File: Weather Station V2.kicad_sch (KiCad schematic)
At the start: 44 parts, among them J1 SOLAR IN, J2 18650, J3 Battery_AUX, J6 USB_C, J7 RYLR998, J8 Breakout, Q1 AO4842, Q2 DMP2240UDM-7, SW1 LED_ENABLE, SW2 EN/RST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

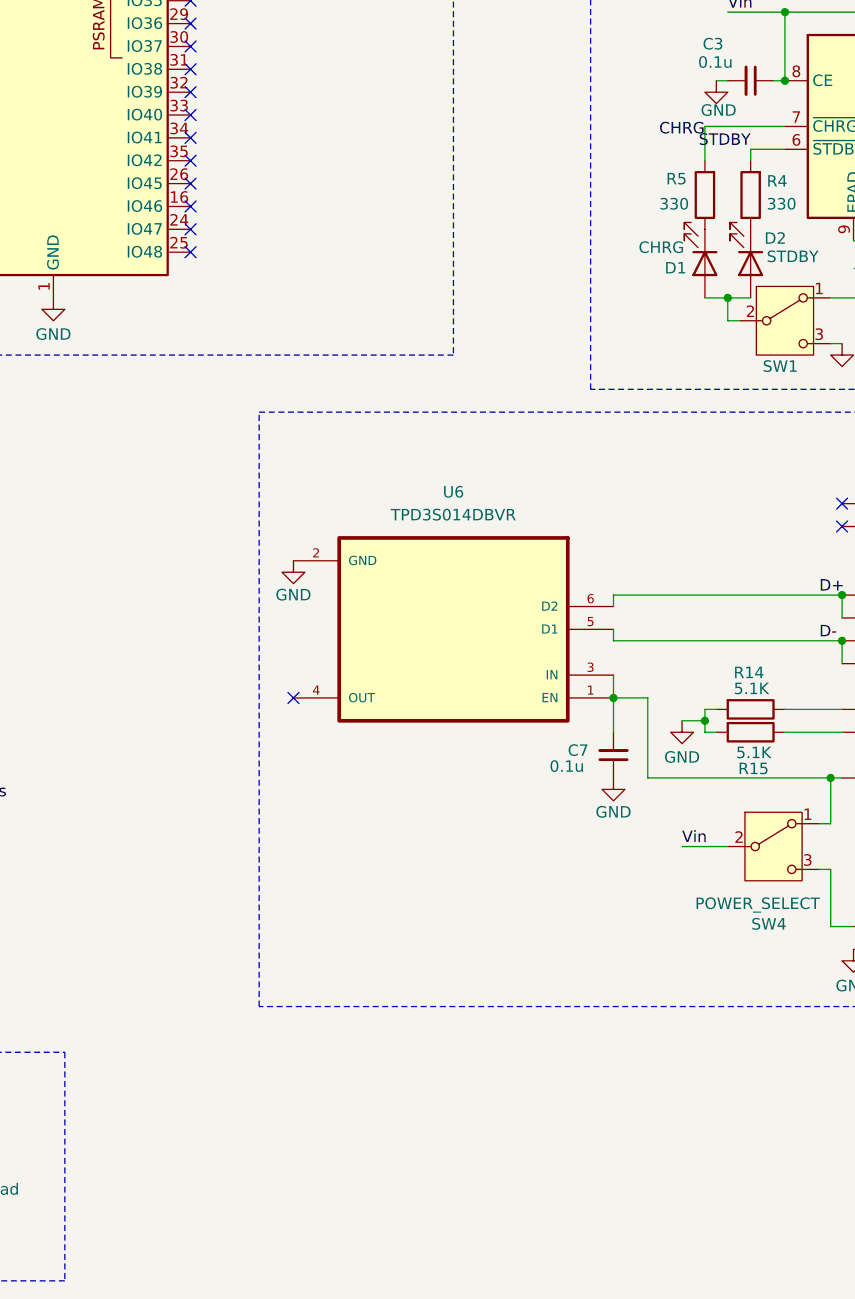
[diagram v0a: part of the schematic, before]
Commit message: Added esp32 connection to charging status lines (CHRG 48, STDBY 47) Panelization with breakout board. Potentially final. Proably sending it soon
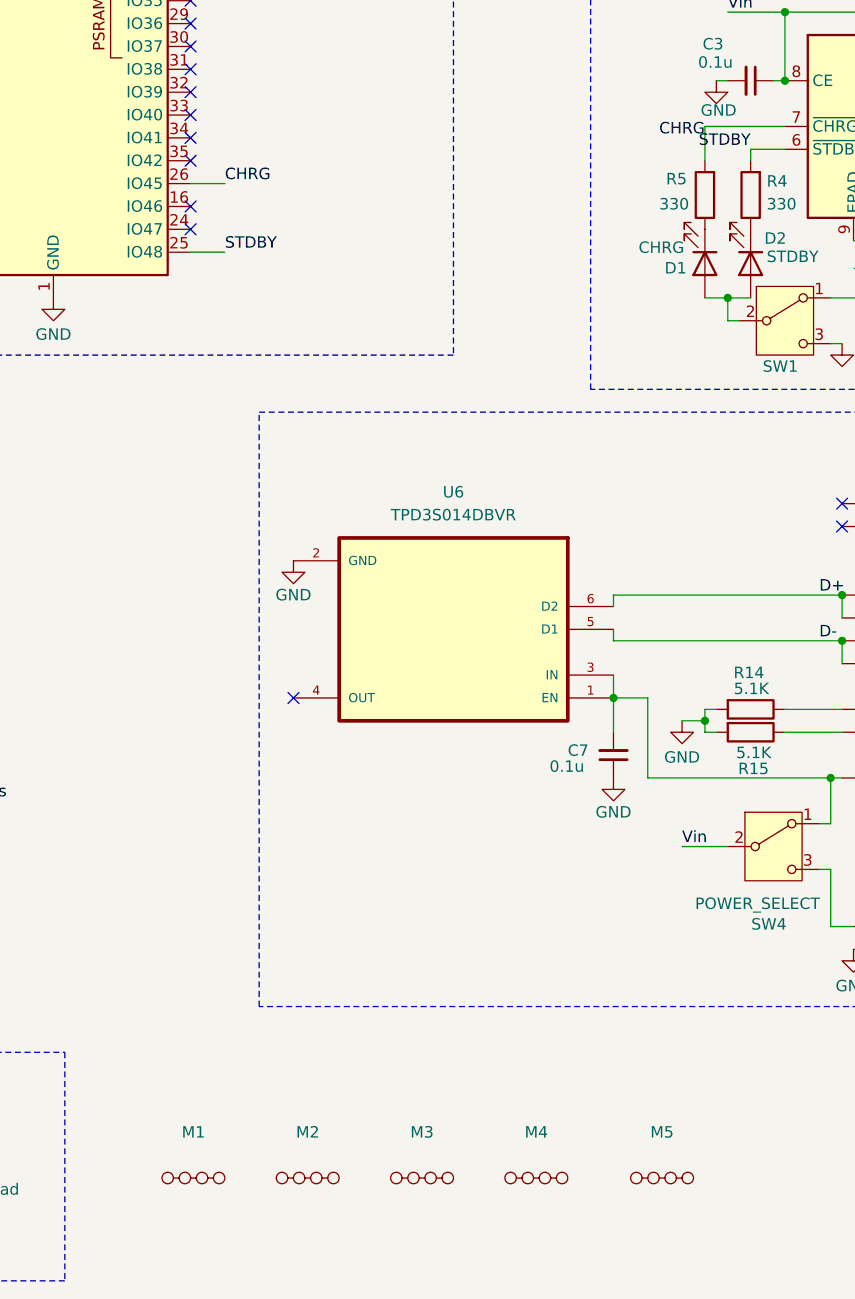
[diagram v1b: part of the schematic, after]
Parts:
- added M1, M2, M3, M4, M5: ~, PCM_JLCPCB:MouseBites, Cosmetic, JLCPCB, 1.6mm, symbol PCM_JLCPCB-Manufacturing:Mousebites, Cosmetic, 3mm
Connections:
- net CHRG: now also U5.26 (IO45)
- net STDBY: now also U5.25 (IO48)
- no-connect marks 22 -> 20

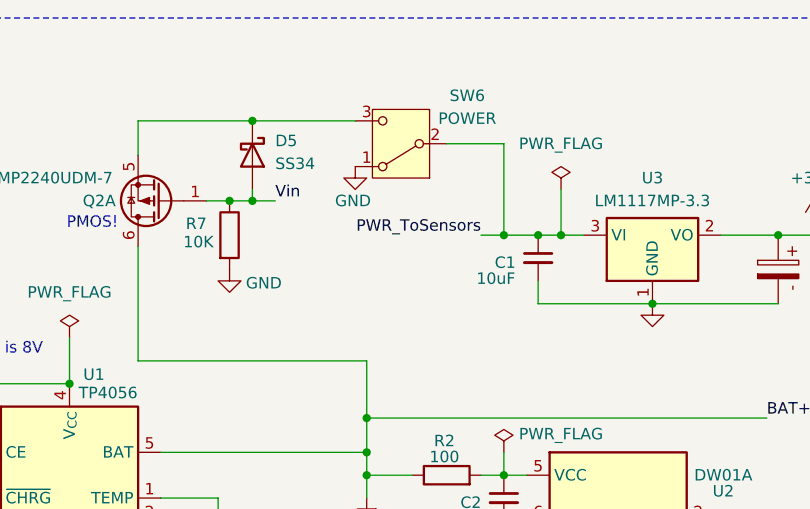
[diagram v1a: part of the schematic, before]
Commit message: Now sensor power gets switched before 5V boost-coverter Reduced 3.3v plane size
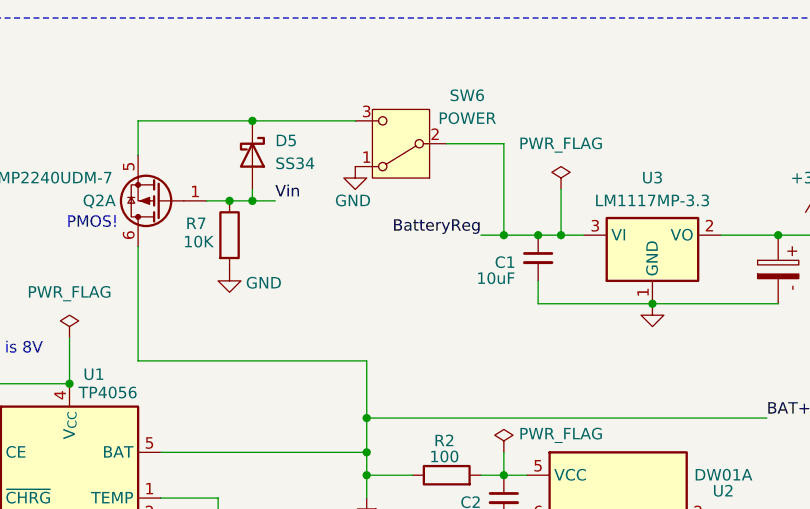
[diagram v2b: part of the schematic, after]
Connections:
- net PWR_ToSensors: no longer C1.1, SW6.2 (B), U3.3 (VI)
- new net BatteryReg: C1.1, SW6.2 (B), U3.3 (VI)
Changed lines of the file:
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@@
 		)
 	)
-	(label "PWR_ToSensors"
+	(label "BatteryReg"
 		(at 236.22 36.83 180)
 		(effects

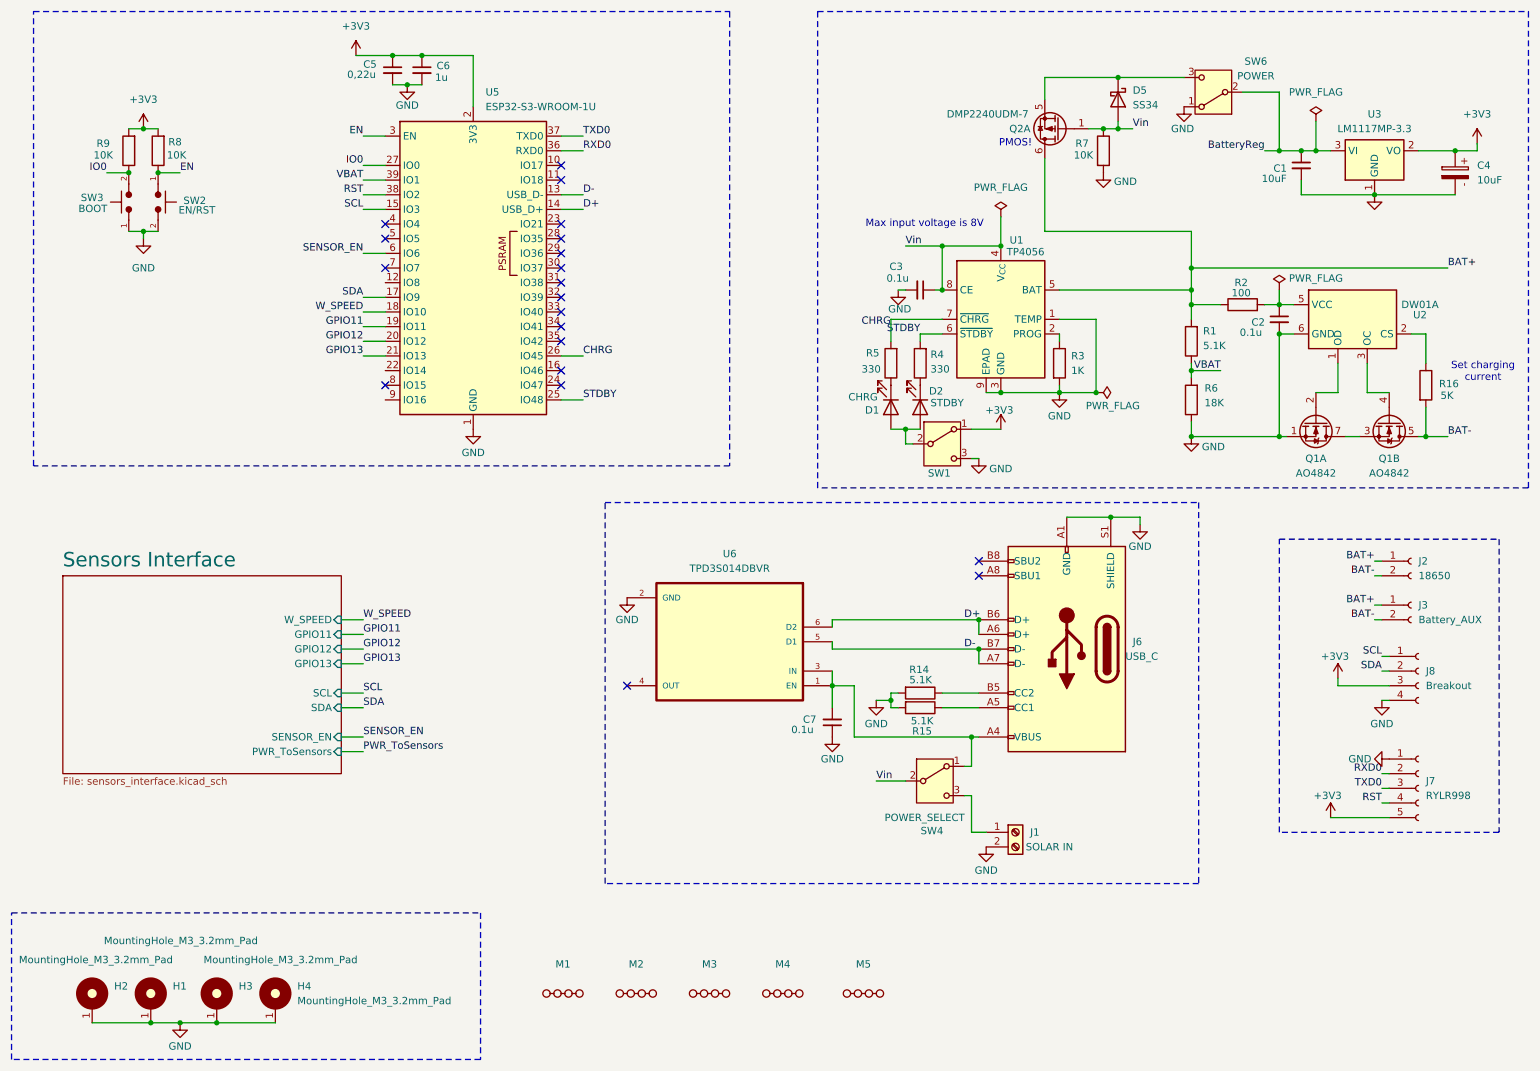
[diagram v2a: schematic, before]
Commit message: - Changed CHRG and STDBY pins to 48 and 47 (CHRG was strapping) - Exposed 5V rail do Breakout connector. Now also it matches a bme280 pinout for testing - Renamed BatteryReg net to Battery_SW - Fixed connection to 5V converter - Changed to USBLC6-2SC6 for ESD Protection - Fixed mirrored VEML7700 footprint
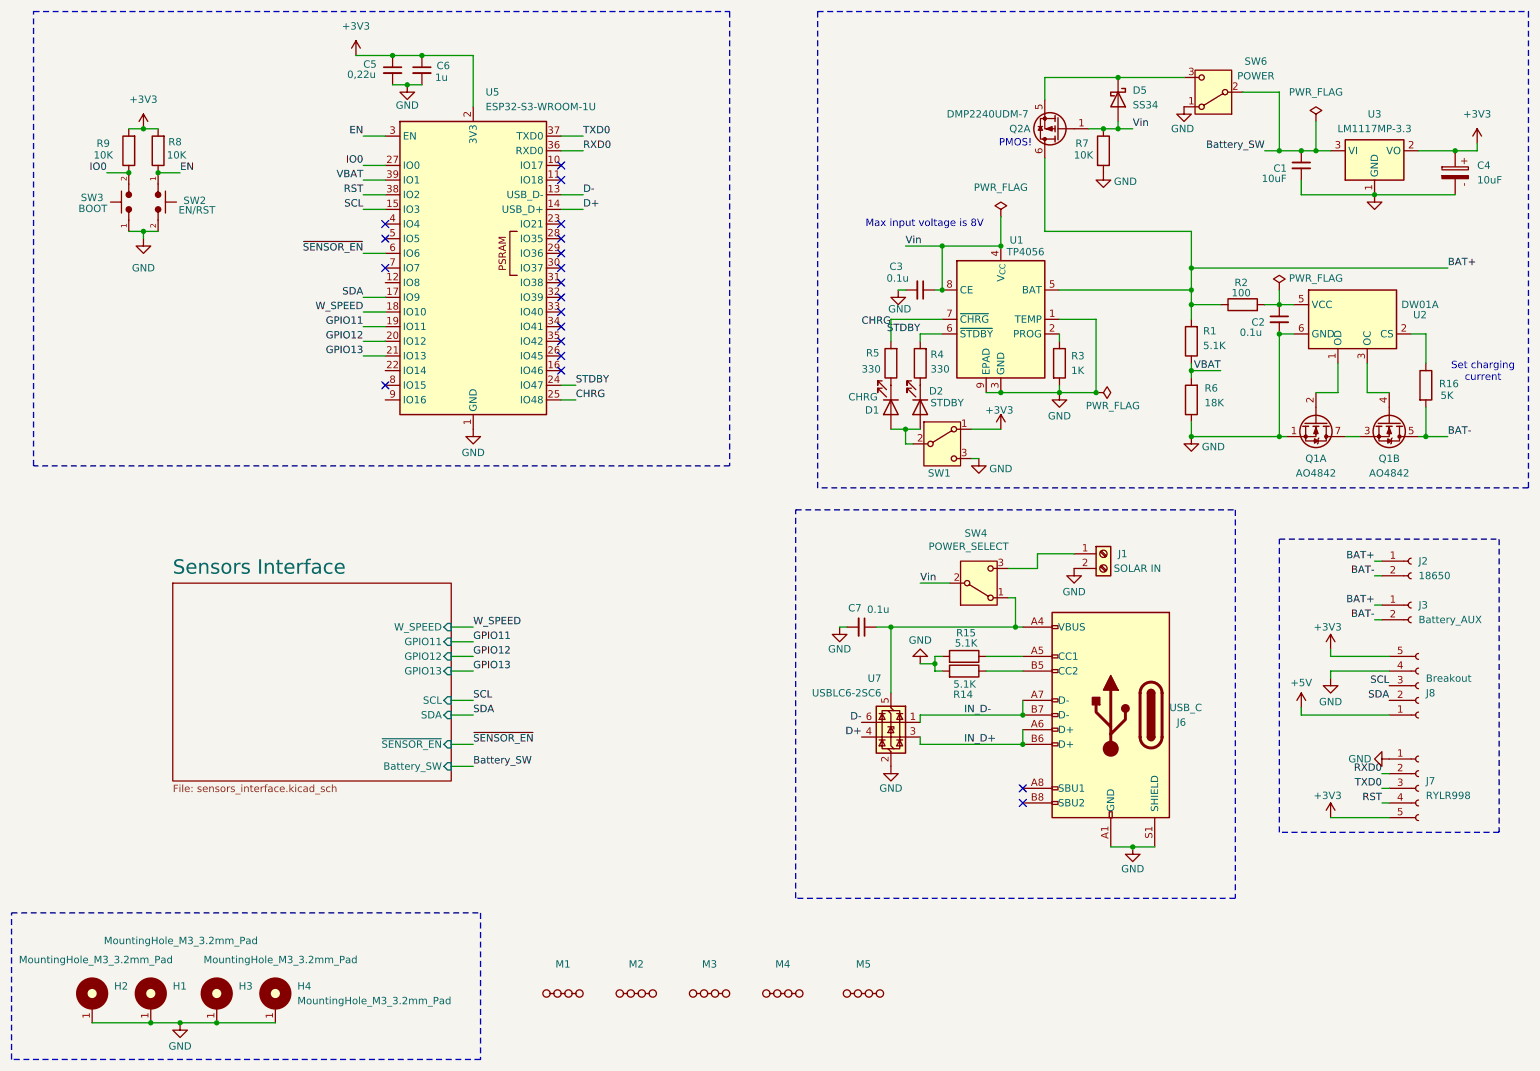
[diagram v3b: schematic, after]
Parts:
- removed J8: Breakout, Connector_PinSocket_2.54mm:PinSocket_1x04_P2.54mm_Vertical, symbol Connector:Conn_01x04_Socket
- removed U6: TPD3S014DBVR, TPD3S014DBVR:SOT95P280X145-6N, symbol TPD3S014DBVR:TPD3S014DBVR
- added J8: Breakout, Connector_PinSocket_2.54mm:PinSocket_1x05_P2.54mm_Vertical, symbol Connector:Conn_01x05_Socket
- added U7: USBLC6-2SC6, Package_TO_SOT_SMD:SOT-23-6, symbol Power_Protection:USBLC6-2SC6
- M1, M2, M3, M4, M5: value ~ -> (none)
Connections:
- net +3V3: now also J8.5 (Pin_5)
- net CHRG: now also U5.25 (IO48); no longer U5.26 (IO45)
- net D+: now also U7.4 (I/O2); no longer J6.A6 (D+), J6.B6 (D+)
- net D-: now also U7.6 (I/O1); no longer J6.A7 (D-), J6.B7 (D-)
- net GND: now also C7.2, J8.4 (Pin_4), U7.2 (GND); no longer C7.1
- net SCL: now also J8.3 (Pin_3)
- net SDA: now also J8.2 (Pin_2)
- net STDBY: now also U5.24 (IO47); no longer U5.25 (IO48)
- net at J6.A4 (VBUS), J6.A9 (VBUS), J6.B4 (VBUS)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: now also C7.1, U7.5 (VBUS); no longer C7.2
- net BatteryReg renamed Battery_SW
- net SENSOR_EN renamed ~{SENSOR_EN}
- new net +5V: J8.1 (Pin_1)
- new net IN_D+: J6.A6 (D+), J6.B6 (D+), U7.3 (I/O2)
- new net IN_D-: J6.A7 (D-), J6.B7 (D-), U7.1 (I/O1)
- no-connect marks 20 -> 19
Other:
- sheet Sensors Interface ports: added Battery_SW, ~{SENSOR_EN}; removed PWR_ToSensors, SENSOR_EN
- moved on the sheet: J1, J6, R14, R15, SW4

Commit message: - Changed 3V3 LDO to LDL1117S33R - In a previous commit ON OFF power lables were switched
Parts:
- removed C4: 10uF, Capacitor_THT:CP_Radial_D5.0mm_P2.00mm, symbol PCM_SL_Capacitors:10uF_50V
- added C4: 4.7uF, Capacitor_SMD:C_1206_3216Metric, symbol Device:C_Small
- U3: value LM1117MP-3.3 -> LDL1117S33R
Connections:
- net +3V3: now also C4.1
- net GND: now also C4.2
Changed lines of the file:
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@@
 	)
 	(junction
-		(at 269.24 36.83)
-		(diameter 0)
-		(color 0 0 0 0)
-	)
-	(junction
 		(at 43.18 187.96)
 		(diameter 0)
@@
 	)
 	(junction
+		(at 269.24 36.83)
+		(diameter 0)
+		(color 0 0 0 0)
+	)
+	(junction
 		(at 223.52 63.5)
 		(diameter 0)
@@
 	(wire
 		(pts
+			(xy 269.24 36.83) (xy 273.05 36.83)
+		)
+		(stroke
+			(width 0)
+			(type default)
+		)
+	)
+	(wire
+		(pts
 			(xy 238.76 68.58) (xy 241.3 68.58)
 		)
@@
 	(wire
 		(pts
+			(xy 269.24 41.91) (xy 269.24 44.45)
+		)
+		(stroke
+			(width 0)
+			(type default)
+		)
+	)
+	(wire
+		(pts
 			(xy 175.26 87.63) (xy 173.99 87.63)
 		)
@@
 	(wire
 		(pts
-			(xy 269.24 36.83) (xy 273.05 36.83)
-		)
-		(stroke
-			(width 0)
-			(type default)
-		)
-	)
-	(wire
-		(pts
 			(xy 99.06 139.7) (xy 95.25 139.7)
 		)
@@
 			)
 		)
-		(property "Value" "LM1117MP-3.3"
+		(property "Value" "LDL1117S33R"
 			(at 255.27 33.02 0)
 			(show_name no)
@@
 	)
 	(symbol
-		(lib_id "PCM_SL_Capacitors:10uF_50V")
-		(at 269.24 40.64 270)
-		(unit 1)
-		(body_style 1)
-		(exclude_from_sim no)
-		(in_bom yes)
-		(on_board yes)
-		(in_pos_files yes)
-		(dnp no)
-		(fields_autoplaced yes)
-		(property "Reference" "C4"
-			(at 273.05 39.3699 90)
-			(show_name no)
-			(do_not_autoplace no)
-			(effects
-				(font
-					(size 1.27 1.27)
-				)
-				(justify left)
-			)
-		)
-		(property "Value" "10uF"
-			(at 273.05 41.9099 90)
-			(show_name no)
-			(do_not_autoplace no)
-			(effects
-				(font
-					(size 1.27 1.27)
-				)
-				(justify left)
-			)
-		)
-		(property "Footprint" "Capacitor_THT:CP_Radial_D5.0mm_P2.00mm"
-			(at 265.43 41.402 0)
-			(hide yes)
-			(show_name no)
-			(do_not_autoplace no)
-			(effects
-				(font
-					(size 1.27 1.27)
-				)
-			)
-		)
-		(property "Datasheet" ""
-			(at 269.24 41.148 0)
-			(hide yes)
-			(show_name no)
-			(do_not_autoplace no)
-			(effects
-				(font
-					(size 1.27 1.27)
-				)
-			)
-		)
-		(property "Description" "10uF, 50V Electrolytic Capacitor"
-			(at 269.24 40.64 0)
-			(hide yes)
-			(show_name no)
-			(do_not_autoplace no)
-			(effects
-				(font
-					(size 1.27 1.27)
-				)
-			)
-		)
-		(pin "2"
-		)
-		(pin "1"
-		)
-		(instances
-			(project "Weather Station V2"
-				(path "/817e54af-ab8f-4cfe-9b63-ceac8d6d2a44"
-					(reference "C4")
-					(unit 1)
-				)
-			)
-		)
-	)
-	(symbol
 		(lib_id "power:+3V3")
 		(at 190.5 85.09 0)
@@
 					(unit 1)
 				)
+			)
+		)
+	)
+	(symbol
+		(lib_id "Device:C_Small")
+		(at 269.24 39.37 0)
+		(unit 1)
+		(body_style 1)
+		(exclude_from_sim no)
+		(in_bom yes)
+		(on_board yes)
+		(in_pos_files yes)
+		(dnp no)
+		(property "Reference" "C4"
+			(at 264.414 39.878 0)
+			(show_name no)
+			(do_not_autoplace no)
+			(effects
+				(font
+					(size 1.27 1.27)
+				)
+				(justify left)
+			)
+		)
+		(property "Value" "4.7uF"
+			(at 262.382 41.656 0)
+			(show_name no)
+			(do_not_autoplace no)
+			(effects
+				(font
+					(size 1.27 1.27)
+				)
+				(justify left)
+			)
+		)
+		(property "Footprint" "Capacitor_SMD:C_1206_3216Metric"
+			(at 269.24 39.37 0)
+			(hide yes)
+			(show_name no)
+			(do_not_autoplace no)
+			(effects
+				(font
+					(size 1.27 1.27)
+				)
+			)
+		)
+		(property "Datasheet" ""
+			(at 269.24 39.37 0)
+			(hide yes)
+			(show_name no)
+			(do_not_autoplace no)
+			(effects
+				(font
+					(size 1.27 1.27)
+				)
+			)
+		)
+		(property "Description" "Unpolarized capacitor, small symbol"
+			(at 269.24 39.37 0)
+			(hide yes)
+			(show_name no)
+			(do_not_autoplace no)
+			(effects
+				(font
+					(size 1.27 1.27)
+				)
+			)
+		)
+		(pin "1"
+		)
+		(pin "2"
+		)
+		(instances
+			(project "Weather Station V2"
+				(path "/817e54af-ab8f-4cfe-9b63-ceac8d6d2a44"
+					(reference "C4")
+					(unit 1)
+				)
